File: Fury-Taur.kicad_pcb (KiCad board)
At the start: 2 copper layers, 78 x 25 mm, 29 parts, among them J1 Pickup, J2 Output, Q1 Bias 20K, Q1 J201, Q2 Bias 20K, Q2 J201, SW1 ALPHA_PUSH_PULL, SW2 SW_SPDT

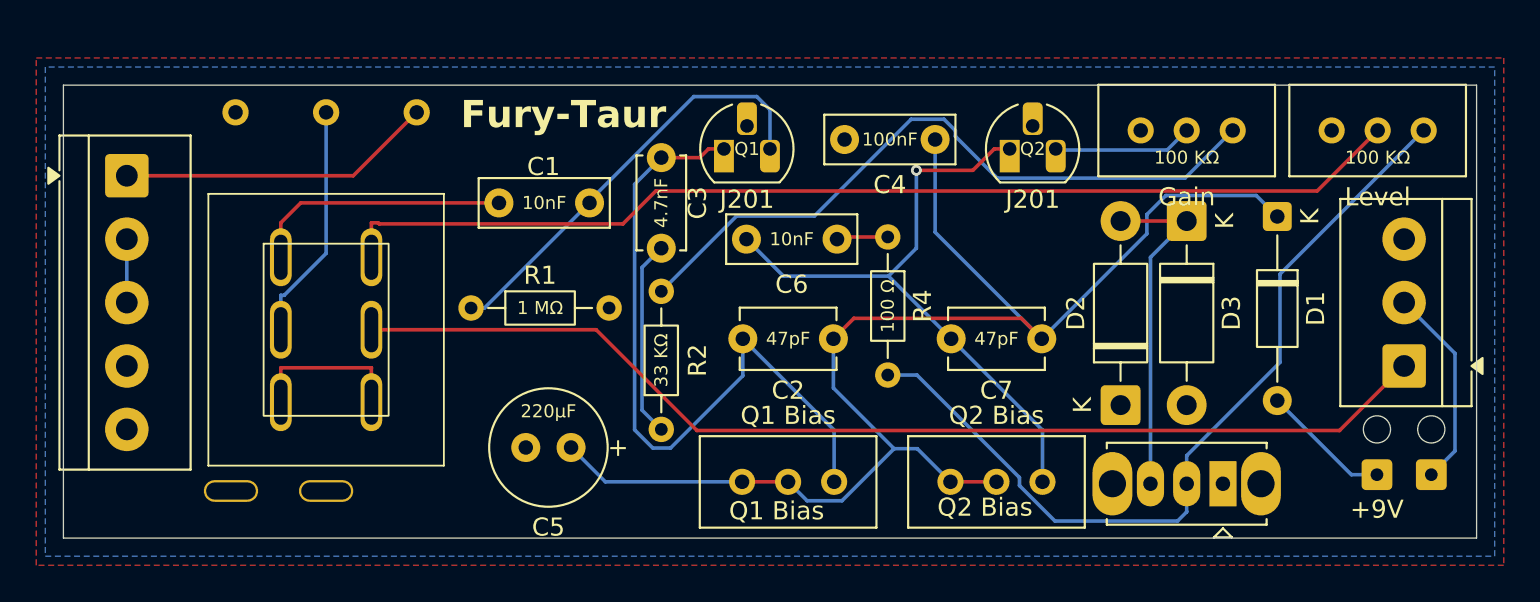
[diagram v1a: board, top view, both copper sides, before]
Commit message: Removed C4, adjusted c5 to 100uf, made PCB slightly smaller
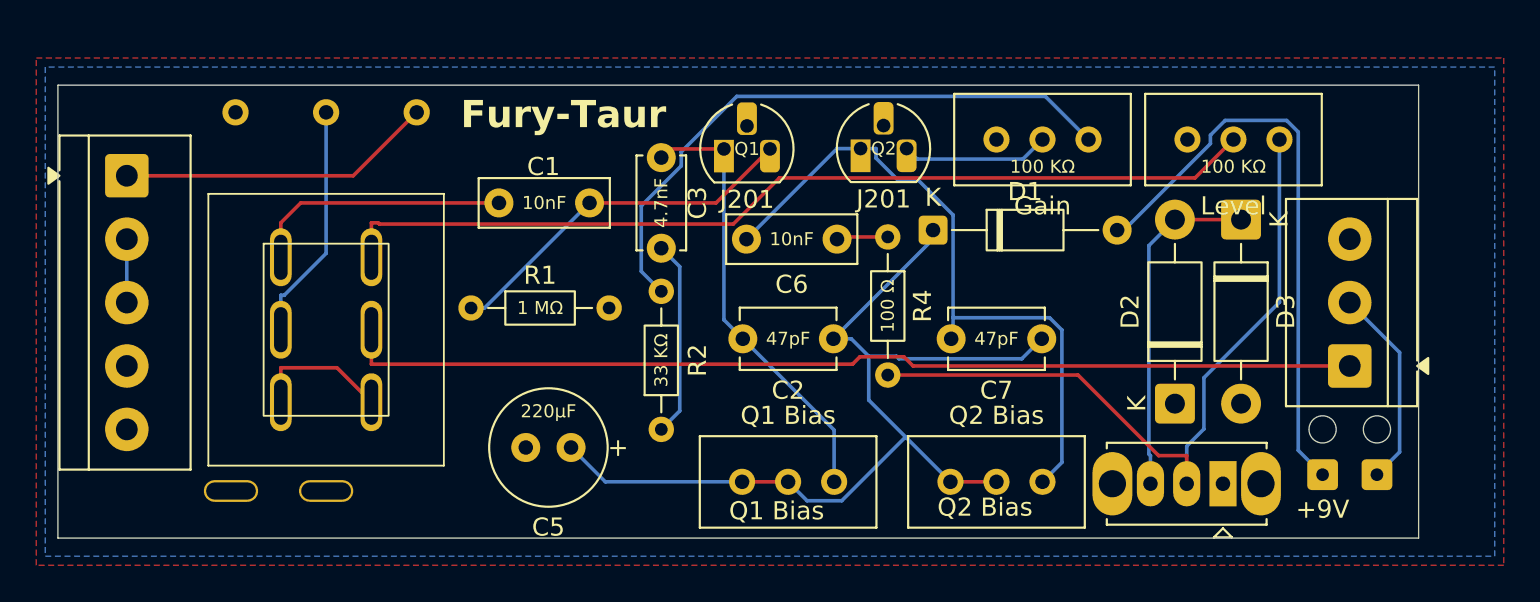
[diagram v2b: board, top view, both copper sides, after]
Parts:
- removed C4: 100nf, Capacitor_THT:C_Disc_D7.0mm_W2.5mm_P5.00mm
- moved D1 19.0 mm to (126.5, 72.0), turned to 0 degrees
- moved Q2 8.23 mm to (122.5, 67.5)
- moved R5 7.98 mm to (145.6, 67.0)
- moved R3 7.98 mm to (135.1, 67.0)
- moved D2 3.00 mm to (139.8, 81.6)
- moved D3 3.00 mm to (143.5, 71.4)
- moved 9V+ 3.00 mm to (148.0, 85.5)
- moved BAT- 3.00 mm to (151.0, 85.5)
- moved J2 3.00 mm to (149.5, 79.5)
- moved TH1 3.00 mm to (148.0, 83.0)
- moved TH2 3.00 mm to (151.0, 83.0)
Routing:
- net +9V: track 7.19 -> 32.5 mm
- net Net-(D1-K): track 77.3 -> 53.2 mm
- net Net-(Q1-D): track 39.4 -> 24.6 mm
- net Net-(R5-Pad2): track 59.6 -> 51.4 mm
- net Net-(SW2-B): track 46.8 -> 41.0 mm
- net VOL_OUT_TO_JACK_TIP: track 60.8 -> 56.3 mm
- net Net-(R2-Pad2): track 38.1 -> 33.8 mm
- net Net-(Q1-G): track 23.9 -> 20.1 mm
- net Net-(Q2-D): track 35.7 -> 37.3 mm, vias 1 -> 0
- net COMMON: track 8.80 -> 7.69 mm
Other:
- board size 78 x 25 mm -> 75.1 x 25 mm

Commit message: Adjusted 47pf and 100uf capacitor footprints
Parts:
- C2, C7: footprint Capacitor_THT:C_Disc_D5.1mm_W3.2mm_P5.00mm -> Capacitor_THT:C_Disc_D4.7mm_W2.5mm_P5.00mm
- C5: value 220μF -> 100μF; footprint Capacitor_THT:C_Radial_D6.3mm_H11.0mm_P2.50mm -> Capacitor_THT:C_Radial_D5.0mm_H11.0mm_P2.00mm
- moved D1 0.38 mm to (126.5, 72.4)

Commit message: Adusted board shape
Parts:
- moved R3 1.02 mm to (134.9, 66.0)
- moved R5 1.00 mm to (145.7, 66.0)
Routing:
- net Net-(D2-A): track 18.9 -> 34.2 mm
- net +9V: track 32.5 -> 17.8 mm
- net VOL_OUT_TO_JACK_TIP: track 56.3 -> 57.9 mm
- net Net-(R2-Pad2): track 33.8 -> 32.3 mm
- net Net-(D1-K): track 53.2 -> 54.4 mm
- net COMMON: track 7.69 -> 8.80 mm
- net Net-(SW2-B): track 41.0 -> 41.7 mm
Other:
- board size 75.1 x 25 mm -> 75.1 x 26.5 mm
